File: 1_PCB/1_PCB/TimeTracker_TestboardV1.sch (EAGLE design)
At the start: 32 parts, among them IC1 7805DT, IC2 7805DT, U1 WS2812B, U2 WS2812B, U3 WS2812B, U4 WS2812B, U5 SMTM1225, Y1 FX135A-327

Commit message: Nico
Update PCB
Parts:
- added C6: 0.1uF, SparkFun-Capacitors:0.1UF-25V(+80/-20%)(0603)
- added C7, C9: 0.1u, rcl:C-EUC0805
- added C8: (no value), rcl:C-EUC0805
- added R10, R11, R12, R13, R4, R5: 10K, rcl:R-EU_R0805
- added SJ4, SJ5: JUMPER-PAD-3-2OF3_NC_BY_TRACE_SMALL, SparkFun-Passives:JUMPER-PAD-3-2OF3_NC_BY_TRACE_SMALL
- added U6: SX1509, SparkFun-DigitalIC:SX1509
- renumbered IC1 to LD1117DT33TR
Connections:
- removed net !CS_3V3: JP6.!CS, R9.1
- removed net CD: JP6.CD2
- removed net N$18: HM1.SCL, R2.1
- removed net RFIDCS: JP1.1, JP3.2
- removed net RFIDRESET: JP1.7, JP2.2
- removed net SDA: HM1.SDA, R1.1
- new net !INT: R10.1, U6.!INT
- new net !RESET: R4.1, U6.!RESET
- new net !SD_CS: JP6.!CS, R9.1, U6.I/O[0]
- new net 10: U6.I/O[10]
- new net 11: U6.I/O[11]
- new net 12: U6.I/O[12]
- new net 13: U6.I/O[13]
- new net 14: U6.I/O[14]
- new net 15: U6.I/O[15]
- new net 4: U6.I/O[4]
- new net 5: U6.I/O[5]
- new net 6: U6.I/O[6]
- new net 7: U6.I/O[7]
- new net 8: U6.I/O[8]
- new net 9: U6.I/O[9]
- new net ADDR0: SJ4.2, U6.ADDR0
- new net ADDR1: SJ5.2, U6.ADDR1
- new net I2CSCL: HM1.SCL, R12.1, R2.1, U$1.A5SCL, U$2.SCL, U6.SCL
- new net I2CSDA: HM1.SDA, R1.1, R13.1, U$1.A4SDA, U$2.SDA, U6.SDA
- new net LED_DIN: U$1.D2, U4.DIN
- new net N$6: R11.1, SJ5.1
- new net N$8: R5.1, SJ4.1
- new net OSCIO: U6.OSCIO
- new net RFID_CS: JP1.1, JP3.2, U6.I/O[2]
- new net RFID_RESET: JP1.7, JP2.2, U6.I/O[3]
- new net SD_CD: JP6.CD2, U6.I/O[1]
- net 3V3: now also C6.1, C7.1, C8.1, C9.1, R10.2, R11.2, R12.2, R13.2, R4.2, R5.2, R8.2, U6.VCC1, U6.VCC2, U6.VDDM
- net 5V: no longer R8.2
- net GND: now also C6.2, C7.2, C8.2, C9.2, SJ4.3, SJ5.3, U6.GND
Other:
- moved on the sheet: JP4, JP5, JP6, R1, R2, R6, R7, R8, R9, RESET1

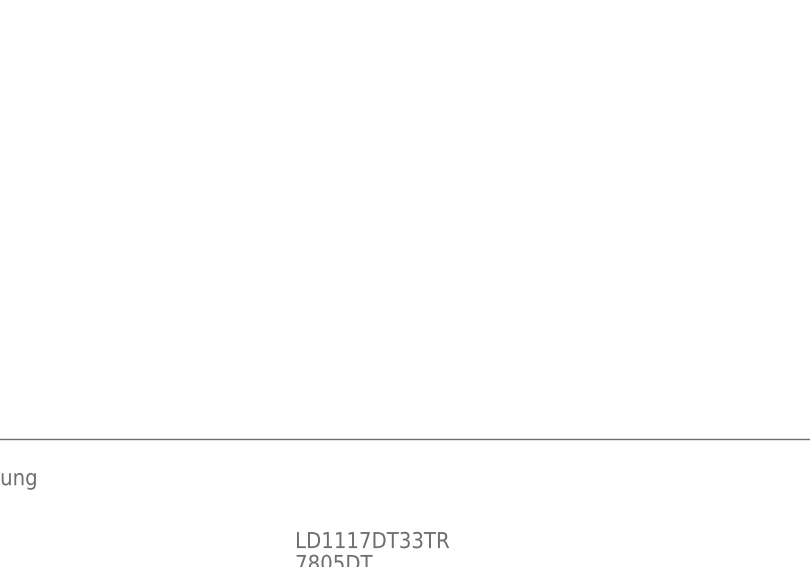
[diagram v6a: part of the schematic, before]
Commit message: Added a new Voltage Regulator
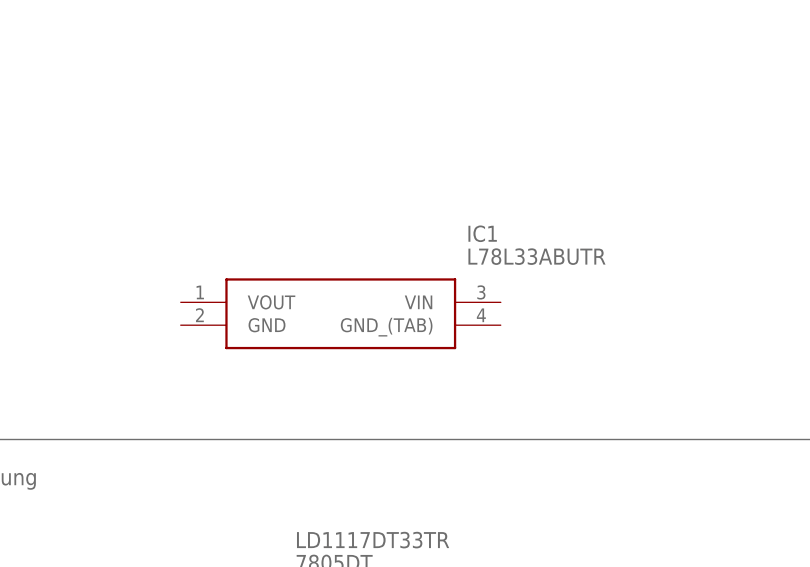
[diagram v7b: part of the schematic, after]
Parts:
- added IC1: L78L33ABUTR, SamacSys_Parts:L78L33ABUTR
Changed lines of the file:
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@@
 <?xml version="1.0" encoding="utf-8"?>
 <!DOCTYPE eagle SYSTEM "eagle.dtd">
-<eagle version="9.3.0">
+<eagle version="9.2.2">
 <drawing>
 <settings>
@@
 <part name="C8" library="rcl" library_urn="urn:adsk.eagle:library:334" deviceset="C-EU" device="C0805" package3d_urn="urn:adsk.eagle:package:23617/2"/>
 <part name="GND20" library="supply1" library_urn="urn:adsk.eagle:library:371" deviceset="GND" device=""/>
+<part name="IC1" library="SamacSys_Parts" deviceset="L78L33ABUTR" device=""/>
 </parts>
 <sheets>
@@
 <attribute name="VALUE" x="137.16" y="162.56" size="1.778" layer="96"/>
 </instance>
+<instance part="IC1" gate="G$1" x="-193.04" y="220.98" smashed="yes">
+<attribute name="NAME" x="-161.29" y="228.6" size="1.778" layer="95" align="center-left"/>
+<attribute name="VALUE" x="-161.29" y="226.06" size="1.778" layer="96" align="center-left"/>
+</instance>
 </instances>

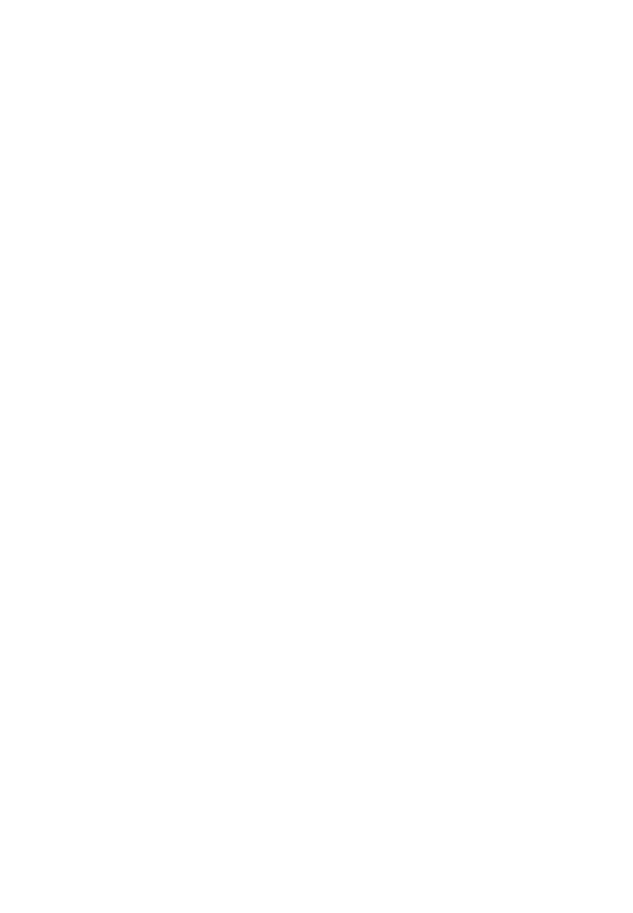
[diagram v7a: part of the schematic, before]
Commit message: I/O Expander changed
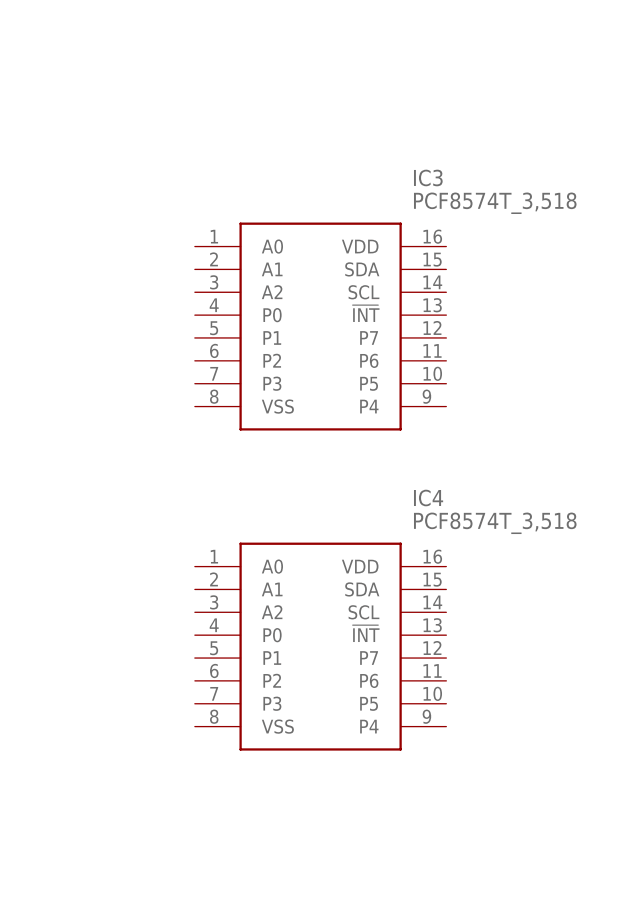
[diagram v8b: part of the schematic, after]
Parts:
- added IC3, IC4: PCF8574T_3,518, SamacSys_Parts:PCF8574T_3,518
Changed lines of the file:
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@@
 <part name="GND20" library="supply1" library_urn="urn:adsk.eagle:library:371" deviceset="GND" device=""/>
 <part name="IC1" library="SamacSys_Parts" deviceset="L78L33ABUTR" device=""/>
+<part name="IC3" library="SamacSys_Parts" deviceset="PCF8574T_3,518" device=""/>
+<part name="IC4" library="SamacSys_Parts" deviceset="PCF8574T_3,518" device=""/>
 </parts>
 <sheets>
@@
 <attribute name="VALUE" x="-161.29" y="226.06" size="1.778" layer="96" align="center-left"/>
 </instance>
+<instance part="IC3" gate="G$1" x="309.88" y="160.02" smashed="yes">
+<attribute name="NAME" x="334.01" y="167.64" size="1.778" layer="95" align="center-left"/>
+<attribute name="VALUE" x="334.01" y="165.1" size="1.778" layer="96" align="center-left"/>
+</instance>
+<instance part="IC4" gate="G$1" x="309.88" y="124.46" smashed="yes">
+<attribute name="NAME" x="334.01" y="132.08" size="1.778" layer="95" align="center-left"/>
+<attribute name="VALUE" x="334.01" y="129.54" size="1.778" layer="96" align="center-left"/>
+</instance>
 </instances>
